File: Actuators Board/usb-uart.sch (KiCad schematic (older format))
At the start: 15 parts

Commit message: fixed CP2102 connections
added polarised capacitors, deleted old CP and added hierarchical pin
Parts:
- removed D?: D_Schottky, Diode_SMD:D_SOD-123F, symbol Device:D_Schottky
- removed R?: 22.1k, symbol Device:R_Small
- removed R?: 47.5k, symbol Device:R_Small
- removed R?: 22K, Resistor_SMD:R_0603_1608Metric, symbol Device:R_Small
- removed R?: 43K, Resistor_SMD:R_0603_1608Metric, symbol Device:R_Small
- removed R?: 1K, Resistor_SMD:R_0603_1608Metric, symbol Device:R_Small
- removed U?: CP2102N-A01-GQFN24, Package_DFN_QFN:QFN-24-1EP_4x4mm_P0.5mm_EP2.6x2.6mm_ThermalVias, symbol Interface_USB:CP2102N-A01-GQFN24
- added C?: 0.1uF, symbol Device:C_Small
- added C?: 4.7uF, symbol Device:CP1_Small
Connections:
- net labels added: 3.3V
- net labels removed: VDD
- wire segments 77 -> 46
- no-connect marks 19 -> 20

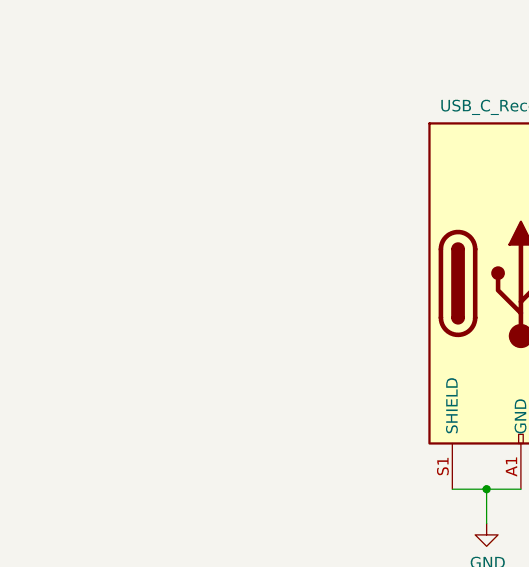
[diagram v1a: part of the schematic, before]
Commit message: Added Data+, Data- and VBUS test points
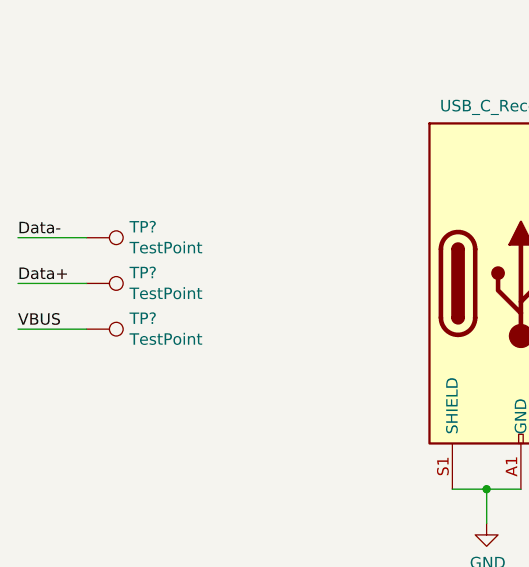
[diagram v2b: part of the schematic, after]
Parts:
- added TP? (x3): TestPoint, symbol Connector:TestPoint
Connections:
- net Data+: now also TP?.1
- net Data-: now also TP?.1
- net VBUS: now also TP?.1
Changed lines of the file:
@@
 Wire Wire Line
 	3850 1750 4400 1750
+$Comp
+L Connector:TestPoint TP?
+U 1 1 61AB7CB8
+P 2050 3900
+F 0 "TP?" V 2004 4088 50  0000 L CNN
+F 1 "TestPoint" V 2095 4088 50  0000 L CNN
+F 2 "" H 2250 3900 50  0001 C CNN
+F 3 "~" H 2250 3900 50  0001 C CNN
+	1    2050 3900
+	0    1    1    0
+$EndComp
+$Comp
+L Connector:TestPoint TP?
+U 1 1 61AB87F3
+P 2050 4100
+F 0 "TP?" V 2004 4288 50  0000 L CNN
+F 1 "TestPoint" V 2095 4288 50  0000 L CNN
+F 2 "" H 2250 4100 50  0001 C CNN
+F 3 "~" H 2250 4100 50  0001 C CNN
+	1    2050 4100
+	0    1    1    0
+$EndComp
+$Comp
+L Connector:TestPoint TP?
+U 1 1 61AB9568
+P 2050 4300
+F 0 "TP?" V 2004 4488 50  0000 L CNN
+F 1 "TestPoint" V 2095 4488 50  0000 L CNN
+F 2 "" H 2250 4300 50  0001 C CNN
+F 3 "~" H 2250 4300 50  0001 C CNN
+	1    2050 4300
+	0    1    1    0
+$EndComp
+Text Label 1750 3900 0    50   ~ 0
+Data-
+Wire Wire Line
+	1750 3900 2050 3900
+Text Label 1750 4100 0    50   ~ 0
+Data+
+Wire Wire Line
+	1750 4100 2050 4100
+Text Label 1750 4300 0    50   ~ 0
+VBUS
+Wire Wire Line
+	1750 4300 2050 4300
 $EndSCHEMATC

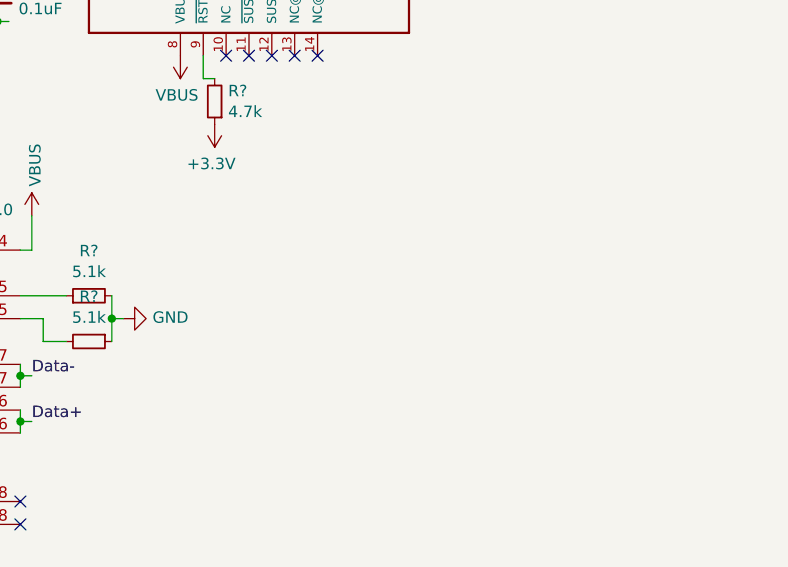
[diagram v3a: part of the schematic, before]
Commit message: Changed main connector to 5 pins, added cool LEDs (needlevalveboard)
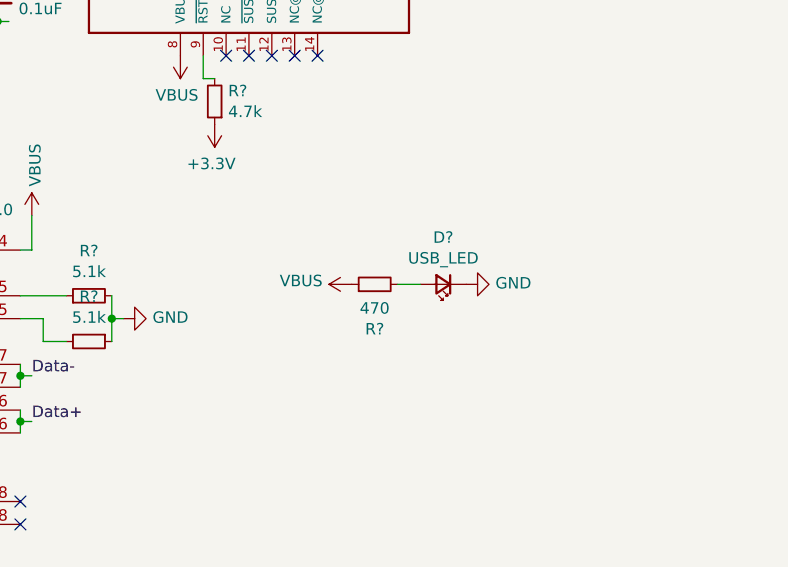
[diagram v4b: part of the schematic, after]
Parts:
- added D?: USB_LED, LED_SMD:LED_0603_1608Metric_Castellated, symbol Device:LED_Small
- added R?: 470, Resistor_SMD:R_0603_1608Metric, symbol Device:R_Small
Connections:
- net GND: now also D?.1 (K)
- net VBUS: now also R?.1
- new net: D?.2 (A), R?.2
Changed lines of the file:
@@
 $Descr A4 11693 8268
 encoding utf-8
-Sheet 1 4
+Sheet 2 4
 Title ""
 Date ""
@@
 Wire Wire Line
 	1750 4300 2050 4300
+$Comp
+L Device:LED_Small D?
+U 1 1 61B104EA
+P 6400 3650
+AR Path="/61B104EA" Ref="D?"  Part="1"
+AR Path="/61925999/61B104EA" Ref="D?"  Part="1"
+F 0 "D?" H 6400 3445 50  0000 C CNN
+F 1 "USB_LED" H 6400 3536 50  0000 C CNN
+F 2 "LED_SMD:LED_0603_1608Metric_Castellated" V 6400 3650 50  0001 C CNN
+F 3 "~" V 6400 3650 50  0001 C CNN
+	1    6400 3650
+	-1   0    0    1
+$EndComp
+$Comp
+L Device:R_Small R?
+U 1 1 61B104F0
+P 6100 3650
+F 0 "R?" V 5904 3650 50  0000 C CNN
+F 1 "470" V 5995 3650 50  0000 C CNN
+F 2 "Resistor_SMD:R_0603_1608Metric" H 6100 3650 50  0001 C CNN
+F 3 "~" H 6100 3650 50  0001 C CNN
+	1    6100 3650
+	0    -1   -1   0
+$EndComp
+Wire Wire Line
+	6300 3650 6200 3650
+$Comp
+L power:GND #PWR?
+U 1 1 61B11F2F
+P 6500 3650
+AR Path="/61B11F2F" Ref="#PWR?"  Part="1"
+AR Path="/61925999/61B11F2F" Ref="#PWR?"  Part="1"
+AR Path="/61997866/61B11F2F" Ref="#PWR?"  Part="1"
+F 0 "#PWR?" H 6500 3400 50  0001 C CNN
+F 1 "GND" V 6505 3522 50  0000 R CNN
+F 2 "" H 6500 3650 50  0001 C CNN
+F 3 "" H 6500 3650 50  0001 C CNN
+	1    6500 3650
+	0    -1   -1   0
+$EndComp
+$Comp
+L power:VBUS #PWR?
+U 1 1 61B168A6
+P 6000 3650
+F 0 "#PWR?" H 6000 3500 50  0001 C CNN
+F 1 "VBUS" V 6015 3778 50  0000 L CNN
+F 2 "" H 6000 3650 50  0001 C CNN
+F 3 "" H 6000 3650 50  0001 C CNN
+	1    6000 3650
+	0    -1   -1   0
+$EndComp
 $EndSCHEMATC
